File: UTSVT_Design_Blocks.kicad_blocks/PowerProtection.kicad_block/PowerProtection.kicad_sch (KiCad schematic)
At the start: 14 parts, among them IC1 LM74502DDFR, Q1 PSMN012-100YS, Q2 PSMN012-100YS

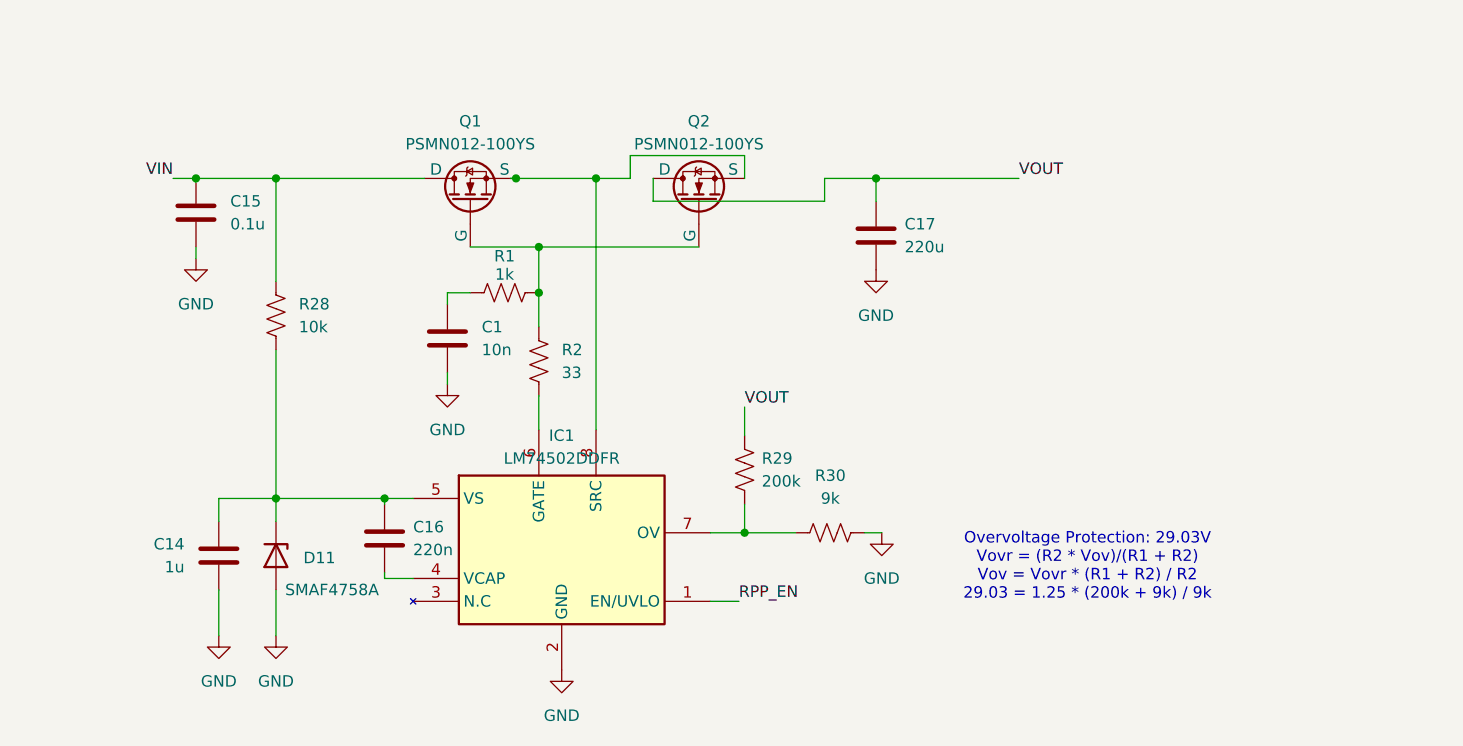
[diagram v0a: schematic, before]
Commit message: unvlo made, updates changed on review file system still bad
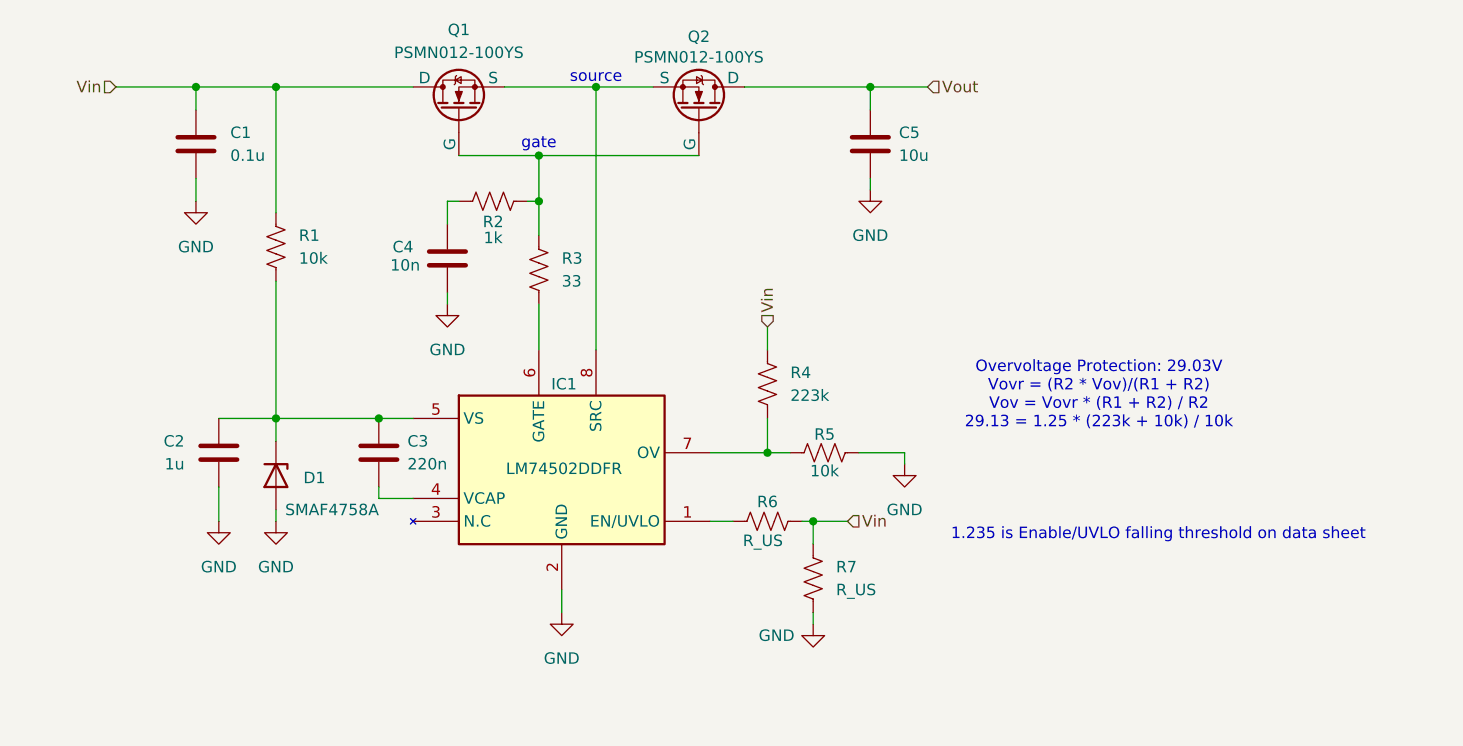
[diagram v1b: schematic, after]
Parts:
- added R6, R7: R_US, symbol Device:R_US
- C5: renamed from C17; value 220u -> 10u
- R4: renamed from R29; value 200k -> 223k
- R5: renamed from R30; value 9k -> 10k
- renumbered C15 to C1, C14 to C2, C16 to C3, C1 to C4, D11 to D1, R28 to R1, R1 to R2, R2 to R3
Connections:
- net GND: now also R7.1
- net RPP_EN: no longer names the net of IC1.1 (EN/UVLO)
- net RPP_EN: now also R6.1
- net VIN renamed Vin
- net Vin: now also R4.1, R6.2, R7.2
- net VOUT renamed Vout
- net Vout: no longer R4.1
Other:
- note added: "1.235 is Enable/UVLO falling threshold on data sheet"
- note added: "Overvoltage Protection: 29.03V Vovr = (R2 * Vov)/(R1 + R2) Vov = Vovr * (R1 + R2) / R2 29.13 = 1.25 * (223k + 10k) / 10k"
- note added: "gate"
- note added: "source"
- note removed: "Overvoltage Protection: 29.03V Vovr = (R2 * Vov)/(R1 + R2) Vov = Vovr * (R1 + R2) / R2 29.03 = 1.25 * (200k + 9k) / 9k"
- moved on the sheet: C1, C2, C3, C4, C5, D1, IC1, Q1, Q2, R1, R2, R3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

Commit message: updated LCSC P/N
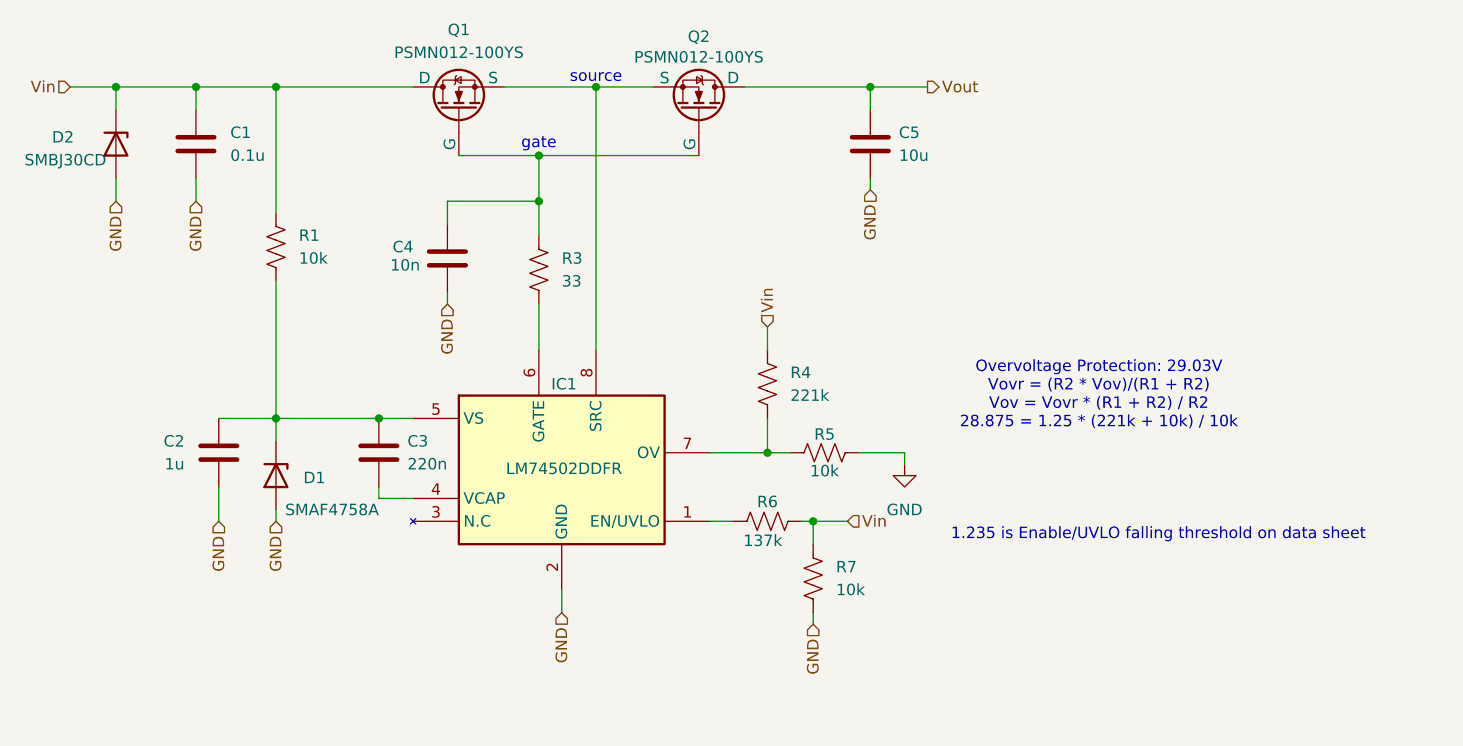
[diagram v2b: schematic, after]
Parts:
- removed Q1, Q2: PSMN012-100YS, symbol Simulation_SPICE:NMOS
- removed R2: 1k, Resistor_SMD:R_0603_1608Metric_Pad0.98x0.95mm_HandSolder, symbol Device:R_US
- added D2: SMBJ30CD, UTSVT_Power:SMBJ30CD, symbol Device:D_Zener
- added Q1, Q2: PSMN012-100YS, UTSVT_Power:PSMN012-100YS, symbol utsvt_power:PSMN012-100YS
- C1: LCSC (none) -> C14663; Mouser Part Number 963-HMK107B7104KA-T -> (none); P/N HMK107B7104KA-T -> MLASH168SB7104KTNA01
- C2: LCSC (none) -> C15849; Mouser Part Number 963-UMK107BJ105KA-T -> (none); P/N UMK107BJ105KA-T -> MLASU168SB5105KTNA01
- C3: LCSC (none) -> C344195
- C4: footprint ECE319K:C_Axial_200mil -> Capacitor_SMD:C_0805_2012Metric_Pad1.18x1.45mm_HandSolder; LCSC (none) -> C57112; P/N (none) -> MSASH168SB5103KTNA01
- C5: LCSC (none) -> C440198; Mouser Part Number 81-GRM21BR61H106KE3K -> (none); P/N MSASU168SB7224KTNB25 -> GRM21BR61H106KE43K
- D1: LCSC (none) -> C779051
- IC1: footprint UTSVT_Power:SOT65P280X110-8N -> UTSVT_Power:LM74502DDFR
- R1: LCSC (none) -> C25804
- R3: LCSC (none) -> C844927
- R4: value 223k -> 221k; LCSC (none) -> C2090661; Mouser Part Number 594-MCT06030C2003FP5 -> (none); P/N MCT06030C2003FP500 -> CRCW0603221KFKEA
- R5: LCSC (none) -> C25804; Mouser Part Number 594-MCT06030C9091FP5 -> (none); P/N MCT06030C9091FP500 -> CRCW060310K0FKEI
- R6: value R_US -> 137k; footprint (none) -> Resistor_SMD:R_0603_1608Metric_Pad0.98x0.95mm_HandSolder; LCSC (none) -> C2090646; P/N (none) -> CRCW0603137KFKEA
- R7: value R_US -> 10k; footprint (none) -> Resistor_SMD:R_0603_1608Metric_Pad0.98x0.95mm_HandSolder; LCSC (none) -> C25804; P/N (none) -> CRCW060310K0FKEI
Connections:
- net GND: now also D2.2 (A)
- net Vin: now also D2.1 (K), Q1.1 (D)
- net Vout: now also Q2.1 (D)
- net at R3.1: now also C4.1, Q1.2 (G), Q2.2 (G)
- net at IC1.8 (SRC): now also Q1.3 (S), Q2.3 (S)
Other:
- note added: "Overvoltage Protection: 29.03V Vovr = (R2 * Vov)/(R1 + R2) Vov = Vovr * (R1 + R2) / R2 28.875 = 1.25 * (221k + 10k) / 10k"
- note removed: "Overvoltage Protection: 29.03V Vovr = (R2 * Vov)/(R1 + R2) Vov = Vovr * (R1 + R2) / R2 29.13 = 1.25 * (223k + 10k) / 10k"

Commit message: embedded datasheets and added hierarchical ground
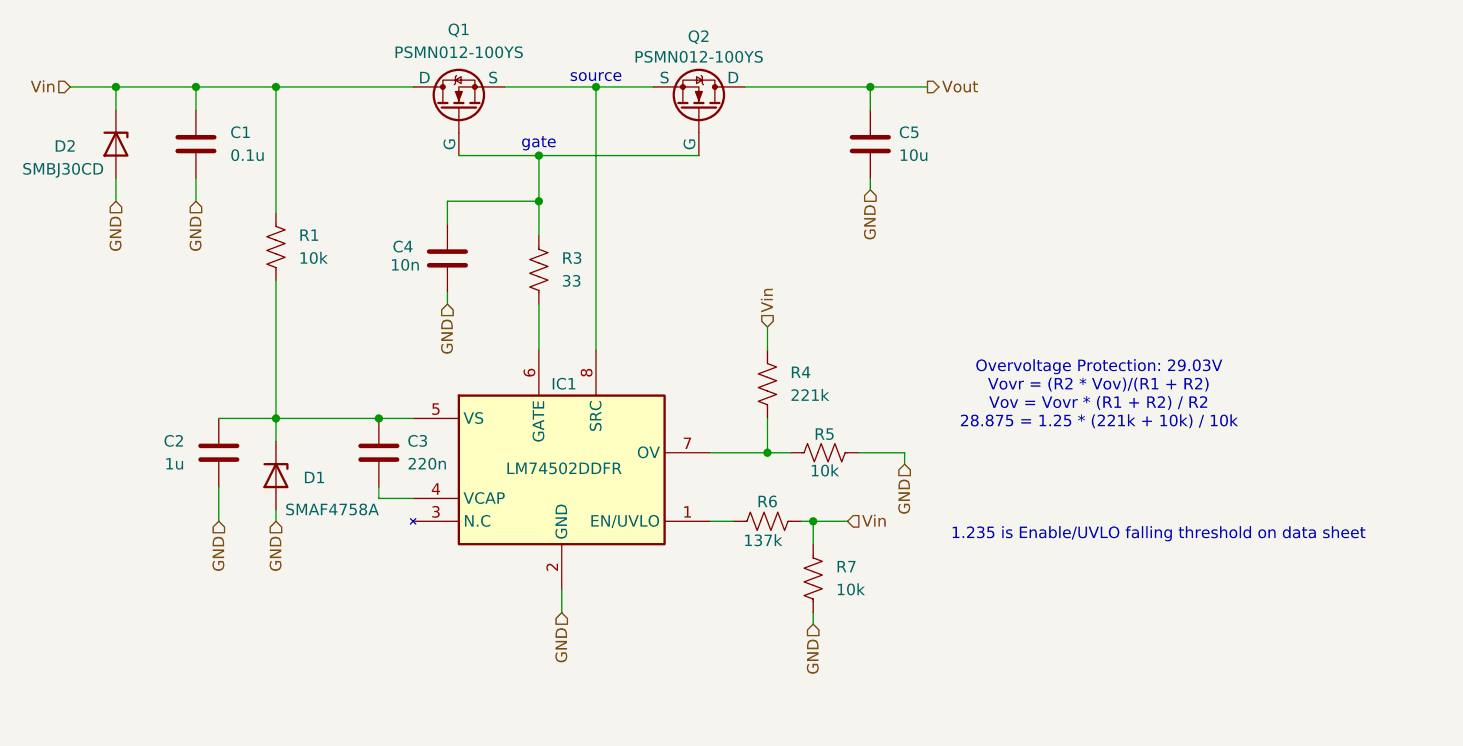
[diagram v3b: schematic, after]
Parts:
- C1: LCSC C14663 -> (none); LCSC P/N (none) -> C14663
- C2: LCSC C15849 -> (none); LCSC P/N (none) -> C15849
- C3: LCSC C344195 -> (none); LCSC P/N (none) -> C344195
- C4: footprint Capacitor_SMD:C_0805_2012Metric_Pad1.18x1.45mm_HandSolder -> Capacitor_SMD:C_0603_1608Metric_Pad1.08x0.95mm_HandSolder; LCSC P/N (none) -> MSASH168SB5103KTNA01; P/N MSASH168SB5103KTNA01 -> (none)
- C5: footprint Capacitor_SMD:C_0805_2012Metric_Pad1.18x1.45mm_HandSolder -> Capacitor_SMD:C_0603_1608Metric_Pad1.08x0.95mm_HandSolder; LCSC C440198 -> (none); LCSC P/N (none) -> C440198
- D1: LCSC C779051 -> (none); LCSC P/N (none) -> C779051
- D2: LCSC C1974995 -> (none); LCSC P/N (none) -> C1974995
- IC1: LCSC P/N (none) -> C3236215
- Q1, Q2: LCSC C20443035 -> (none); LCSC P/N (none) -> C20443035
- R1, R5, R7: LCSC C25804 -> (none); LCSC P/N (none) -> C25804
- R3: LCSC C844927 -> (none); LCSC P/N (none) -> C844927
- R4: LCSC C2090661 -> (none); LCSC P/N (none) -> C2090661
- R6: LCSC C2090646 -> (none); LCSC P/N (none) -> C2090646
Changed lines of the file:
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@@
+	(hierarchical_label "GND"
+		(shape input)
+		(at 113.03 82.55 270)
+		(effects
+			(font
+				(size 1.27 1.27)
+			)
+			(justify right)
+		)
+	)
 	(hierarchical_label "GND"
 		(shape input)
@@
 			)
 		)
-		(property "LCSC" "C344195"
+		(property "LCSC P/N" "C344195"
 			(at 54.61 81.28 0)
 			(effects
@@
 			)
 		)
-		(property "Datasheet" "https://ngspice.sourceforge.io/docs/ngspice-html-manual/manual.xhtml#cha_MOSFETs"
+		(property "Datasheet" "kicad-embed://PSMN012-100YS.pdf"
 			(at 102.87 43.18 0)
 			(effects
@@
 			)
 		)
-		(property "LCSC" "C20443035"
+		(property "LCSC P/N" "C20443035"
 			(at 90.17 43.18 90)
 			(effects
@@
 			)
 		)
-		(property "LCSC" "C25804"
+		(property "LCSC P/N" "C25804"
 			(at 43.18 58.42 0)
 			(effects
@@
 			)
 		)
-		(property "LCSC" "C25804"
+		(property "LCSC P/N" "C25804"
 			(at 102.87 95.25 0)
 			(effects
@@
 			)
 		)
-		(property "LCSC" "C14663"
+		(property "LCSC P/N" "C14663"
 			(at 34.29 46.99 0)
 			(effects
@@
 			)
 		)
-		(property "LCSC" "C2090646"
+		(property "LCSC P/N" "C2090646"
 			(at 97.79 88.9 90)
 			(effects
@@
 			)
 		)
-		(property "LCSC" "C844927"
+		(property "LCSC P/N" "C844927"
 			(at 72.39 60.96 0)
 			(effects
@@
 			)
 		)
-		(property "Datasheet" "https://www.ti.com/lit/ds/symlink/lm74502h.pdf?HQS=dis-mous-null-mousermode-dsf-pf-null-wwe&ts=1659509238199&ref_url=https%253A%252F%252Fwww.mouser.vn%252F"
+		(property "Datasheet" "kicad-embed://LM74502.pdf"
 			(at 87.63 272.39 0)
 			(effects
@@
 			)
 		)
-		(property "If" ""
-			(at 58.42 77.47 0)
-			(effects
-				(font
-					(size 1.27 1.27)
-				)
-				(hide yes)
-			)
-		)
-		(property "Vf" ""
+		(property "LCSC P/N" "C3236215"
 			(at 58.42 77.47 0)
 			(effects
@@
 	)
 	(symbol
+		(lib_name "D_Zener_1")
 		(lib_id "Device:D_Zener")
 		(at 25.4 46.99 270)
@@
 		(dnp no)
 		(property "Reference" "D2"
-			(at 18.288 46.228 90)
+			(at 18.542 47.244 90)
 			(effects
 				(font
@@
 		)
 		(property "Value" "SMBJ30CD"
-			(at 15.24 48.768 90)
+			(at 14.986 49.784 90)
 			(effects
 				(font
@@
 			)
 		)
-		(property "LCSC" "C1974995"
+		(property "LCSC P/N" "C1974995"
 			(at 25.4 46.99 90)
 			(effects
@@
 			)
 		)
-		(property "Datasheet" "https://ngspice.sourceforge.io/docs/ngspice-html-manual/manual.xhtml#cha_MOSFETs"
+		(property "Datasheet" "kicad-embed://PSMN012-100YS.pdf"
 			(at 76.2 43.18 0)
 			(effects
@@
 			)
 		)
-		(property "LCSC" "C20443035"
+		(property "LCSC P/N" "C20443035"
 			(at 63.5 43.18 90)
 			(effects
@@
 			)
 		)
-		(property "Footprint" "Capacitor_SMD:C_0805_2012Metric_Pad1.18x1.45mm_HandSolder"
+		(property "Footprint" "Capacitor_SMD:C_0603_1608Metric_Pad1.08x0.95mm_HandSolder"
 			(at 63.1952 63.5 0)
 			(effects
@@
 			)
 		)
-		(property "P/N" "MSASH168SB5103KTNA01"
+		(property "LCSC P/N" "MSASH168SB5103KTNA01"
 			(at 62.23 59.69 0)
 			(effects
@@
 				(path "/a968d2b9-0c0e-491c-a5a4-aacd8448ff64"
 					(reference "C4")
-					(unit 1)
-				)
-			)
-		)
-	)
-	(symbol
-		(lib_id "power:GND")
-		(at 113.03 82.55 0)
-		(unit 1)
-		(exclude_from_sim no)
-		(in_bom yes)
-		(on_board yes)
-		(dnp no)
-		(fields_autoplaced yes)
-		(property "Reference" "#PWR07"
-			(at 113.03 88.9 0)
-			(effects
-				(font
-					(size 1.27 1.27)
-				)
-				(hide yes)
-			)
-		)
-		(property "Value" "GND"
-			(at 113.03 87.63 0)
-			(effects
-				(font
-					(size 1.27 1.27)
-				)
-			)
-		)
-		(property "Footprint" ""
-			(at 113.03 82.55 0)
-			(effects
-				(font
-					(size 1.27 1.27)
-				)
-				(hide yes)
-			)
-		)
-		(property "Datasheet" ""
-			(at 113.03 82.55 0)
-			(effects
-				(font
-					(size 1.27 1.27)
-				)
-				(hide yes)
-			)
-		)
-		(property "Description" "Power symbol creates a global label with name \"GND\" , ground"
-			(at 113.03 82.55 0)
-			(effects
-				(font
-					(size 1.27 1.27)
-				)
-				(hide yes)
-			)
-		)
-		(pin "1"
-		)
-		(instances
-			(project "PowerProtection"
-				(path "/a968d2b9-0c0e-491c-a5a4-aacd8448ff64"
-					(reference "#PWR07")
 					(unit 1)
 				)
@@
 			)
 		)
-		(property "Footprint" "Capacitor_SMD:C_0805_2012Metric_Pad1.18x1.45mm_HandSolder"
+		(property "Footprint" "Capacitor_SMD:C_0603_1608Metric_Pad1.08x0.95mm_HandSolder"
 			(at 110.1852 50.8 0)
 			(effects
@@
 			)
 		)
-		(property "LCSC" "C440198"
+		(property "LCSC P/N" "C440198"
 			(at 109.22 46.99 0)
 			(effects
@@
 			)
 		)
-		(property "LCSC" "C25804"
+		(property "LCSC P/N" "C25804"
 			(at 104.14 81.28 90)
 			(effects
@@
 			)
 		)
-		(property "Datasheet" "https://www.mouser.com/datasheet/3/225/1/SMAF4735A_SMAF4764A_DO_221AC_.pdf"
+		(property "Datasheet" "kicad-embed://SMAF4735A_SMAF4764A_DO_221AC_.pdf"
 			(at 43.18 83.82 0)
 			(effects
@@
 			)
 		)
-		(property "LCSC" "C779051"
+		(property "LCSC P/N" "C779051"
 			(at 43.18 83.82 90)
 			(effects
@@
 			)
 		)
-		(property "LCSC" "C15849"
+		(property "LCSC P/N" "C15849"
 			(at 36.83 81.28 0)
 			(effects
@@
 			)
 		)
-		(property "LCSC" "C2090661"
+		(property "LCSC P/N" "C2090661"
 			(at 97.79 73.66 0)
 			(effects
